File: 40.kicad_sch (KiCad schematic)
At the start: 54 parts, among them M1 728, M10 PLAIN WASHER_M3, M11 PLAIN WASHER_M3, M12 PLAIN WASHER_M3, M13 PLAIN WASHER_M3, M14 PLAIN WASHER_M3, M19 PLAIN WASHER_M3, M2 728, M3 728, M4 728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

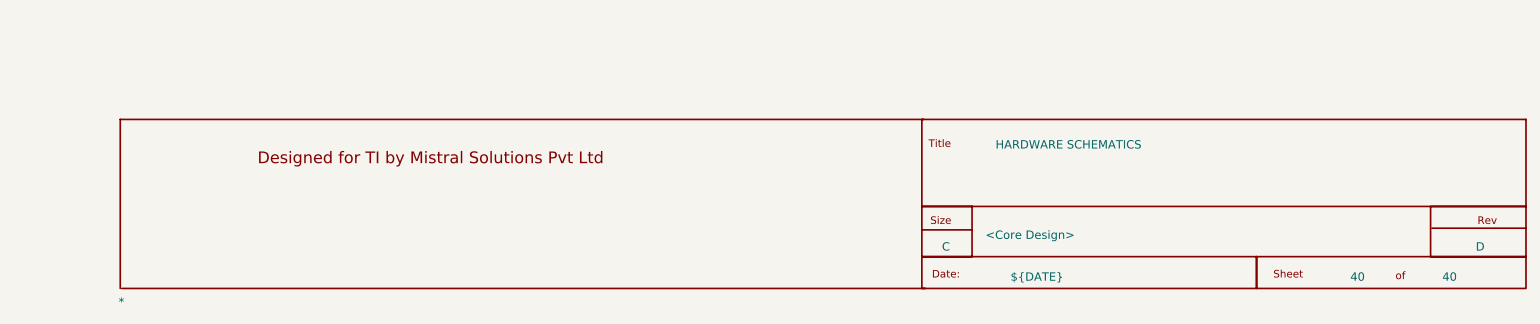
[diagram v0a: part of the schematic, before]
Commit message: fix joint, offpage, and typo
DRC errors are cleared, some warnings remain.
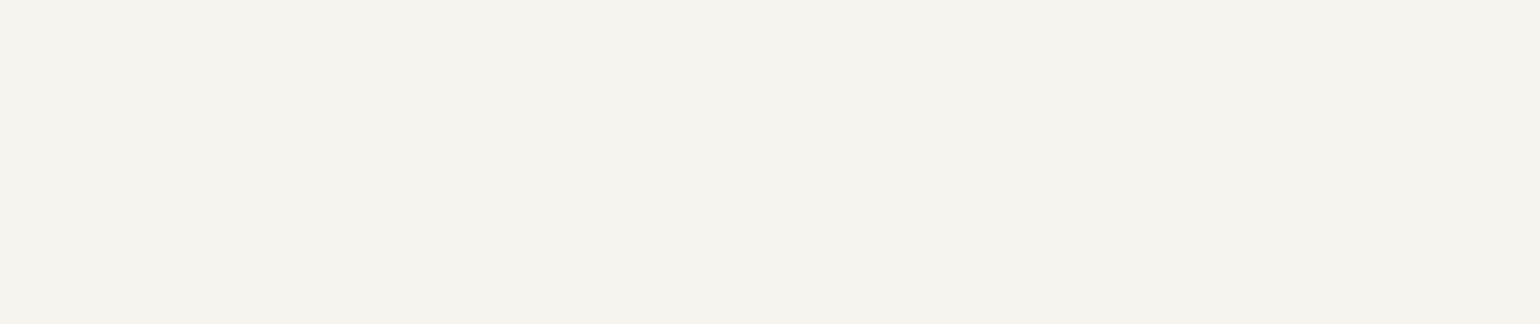
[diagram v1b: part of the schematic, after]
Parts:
- removed *: MISTRAL_TITLEBLK_CSIZE, symbol 40-altium-import:root_0_MISTRAL_TITLEBLK_CSIZE

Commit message: fixpcb.
TODO clean up zones and keepouts on all layers. (top done almost)
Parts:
- removed FID1, FID2, FID3: FID_40X80, Fiducial10-20, symbol 40-altium-import:root_0_Fiducial
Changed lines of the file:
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@@
-	)
-	(symbol
-		(lib_id "40-altium-import:root_0_Fiducial")
-		(at 457.2 121.92 0)
-		(unit 1)
-		(exclude_from_sim no)
-		(in_bom yes)
-		(on_board yes)
-		(dnp no)
-		(property "Reference" "FID2"
-			(at 457.2 129.032 0)
-			(effects
-				(font
-					(size 1.27 1.27)
-				)
-				(justify left bottom)
-			)
-		)
-		(property "Value" "FID_40X80"
-			(at 457.2 132.334 0)
-			(effects
-				(font
-					(size 1.27 1.27)
-				)
-				(justify left bottom)
-			)
-		)
-		(property "Footprint" "Fiducial10-20"
-			(at 457.2 121.92 0)
-			(effects
-				(font
-					(size 1.27 1.27)
-				)
-				(hide yes)
-			)
-		)
-		(property "Datasheet" ""
-			(at 457.2 121.92 0)
-			(effects
-				(font
-					(size 1.27 1.27)
-				)
-				(hide yes)
-			)
-		)
-		(property "Description" ""
-			(at 457.2 121.92 0)
-			(effects
-				(font
-					(size 1.27 1.27)
-				)
-				(hide yes)
-			)
-		)
-		(property "PCB FOOTPRINT" "FID_40X80"
-			(at 0 386.08 0)
-			(effects
-				(font
-					(size 1.27 1.27)
-				)
-				(justify left bottom)
-				(hide yes)
-			)
-		)
-		(instances
-			(project ""
-				(path "/7754ade6-0b9d-4134-a54b-9b646187fb66"
-					(reference "FID2")
-					(unit 1)
-				)
-			)
-			(project ""
-				(path "/d798ab61-bfb1-4e3e-a919-55e6a99857b1/c9416ae5-853a-4adb-8ec6-8b79374967eb"
-					(reference "FID2")
-					(unit 1)
-				)
-			)
-		)
-	)
-	(symbol
-		(lib_id "40-altium-import:root_0_Fiducial")
-		(at 436.88 121.92 0)
-		(unit 1)
-		(exclude_from_sim no)
-		(in_bom yes)
-		(on_board yes)
-		(dnp no)
-		(property "Reference" "FID1"
-			(at 436.88 129.032 0)
-			(effects
-				(font
-					(size 1.27 1.27)
-				)
-				(justify left bottom)
-			)
-		)
-		(property "Value" "FID_40X80"
-			(at 436.88 132.334 0)
-			(effects
-				(font
-					(size 1.27 1.27)
-				)
-				(justify left bottom)
-			)
-		)
-		(property "Footprint" "Fiducial10-20"
-			(at 436.88 121.92 0)
-			(effects
-				(font
-					(size 1.27 1.27)
-				)
-				(hide yes)
-			)
-		)
-		(property "Datasheet" ""
-			(at 436.88 121.92 0)
-			(effects
-				(font
-					(size 1.27 1.27)
-				)
-				(hide yes)
-			)
-		)
-		(property "Description" ""
-			(at 436.88 121.92 0)
-			(effects
-				(font
-					(size 1.27 1.27)
-				)
-				(hide yes)
-			)
-		)
-		(property "PCB FOOTPRINT" "FID_40X80"
-			(at 0 386.08 0)
-			(effects
-				(font
-					(size 1.27 1.27)
-				)
-				(justify left bottom)
-				(hide yes)
-			)
-		)
-		(instances
-			(project ""
-				(path "/7754ade6-0b9d-4134-a54b-9b646187fb66"
-					(reference "FID1")
-					(unit 1)
-				)
-			)
-			(project ""
-				(path "/d798ab61-bfb1-4e3e-a919-55e6a99857b1/c9416ae5-853a-4adb-8ec6-8b79374967eb"
-					(reference "FID1")
-					(unit 1)
-				)
-			)
-		)
 	)
 	(symbol
@@
 					(unit 1)
 				)
-			)
-		)
-	)
-	(symbol
-		(lib_id "40-altium-import:root_0_Fiducial")
-		(at 480.06 121.92 0)
-		(unit 1)
-		(exclude_from_sim no)
-		(in_bom yes)
-		(on_board yes)
-		(dnp no)
-		(property "Reference" "FID3"
-			(at 480.06 129.032 0)
-			(effects
-				(font
-					(size 1.27 1.27)
-				)
-				(justify left bottom)
-			)
-		)
-		(property "Value" "FID_40X80"
-			(at 480.06 132.334 0)
-			(effects
-				(font
-					(size 1.27 1.27)
-				)
-				(justify left bottom)
-			)
-		)
-		(property "Footprint" "Fiducial10-20"
-			(at 480.06 121.92 0)
-			(effects
-				(font
-					(size 1.27 1.27)
-				)
-				(hide yes)
-			)
-		)
-		(property "Datasheet" ""
-			(at 480.06 121.92 0)
-			(effects
-				(font
-					(size 1.27 1.27)
-				)
-				(hide yes)
-			)
-		)
-		(property "Description" ""
-			(at 480.06 121.92 0)
-			(effects
-				(font
-					(size 1.27 1.27)
-				)
-				(hide yes)
-			)
-		)
-		(property "PCB FOOTPRINT" "FID_40X80"
-			(at 0 386.08 0)
-			(effects
-				(font
-					(size 1.27 1.27)
-				)
-				(justify left bottom)
-				(hide yes)
-			)
-		)
-		(instances
-			(project ""
-				(path "/7754ade6-0b9d-4134-a54b-9b646187fb66"
-					(reference "FID3")
-					(unit 1)
-				)
-			)
-			(project ""
-				(path "/d798ab61-bfb1-4e3e-a919-55e6a99857b1/c9416ae5-853a-4adb-8ec6-8b79374967eb"
-					(reference "FID3")
-					(unit 1)
-				)
